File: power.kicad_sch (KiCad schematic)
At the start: 18 parts, among them U4 TPS61040DBV, U5 TPS7A2050PDBV

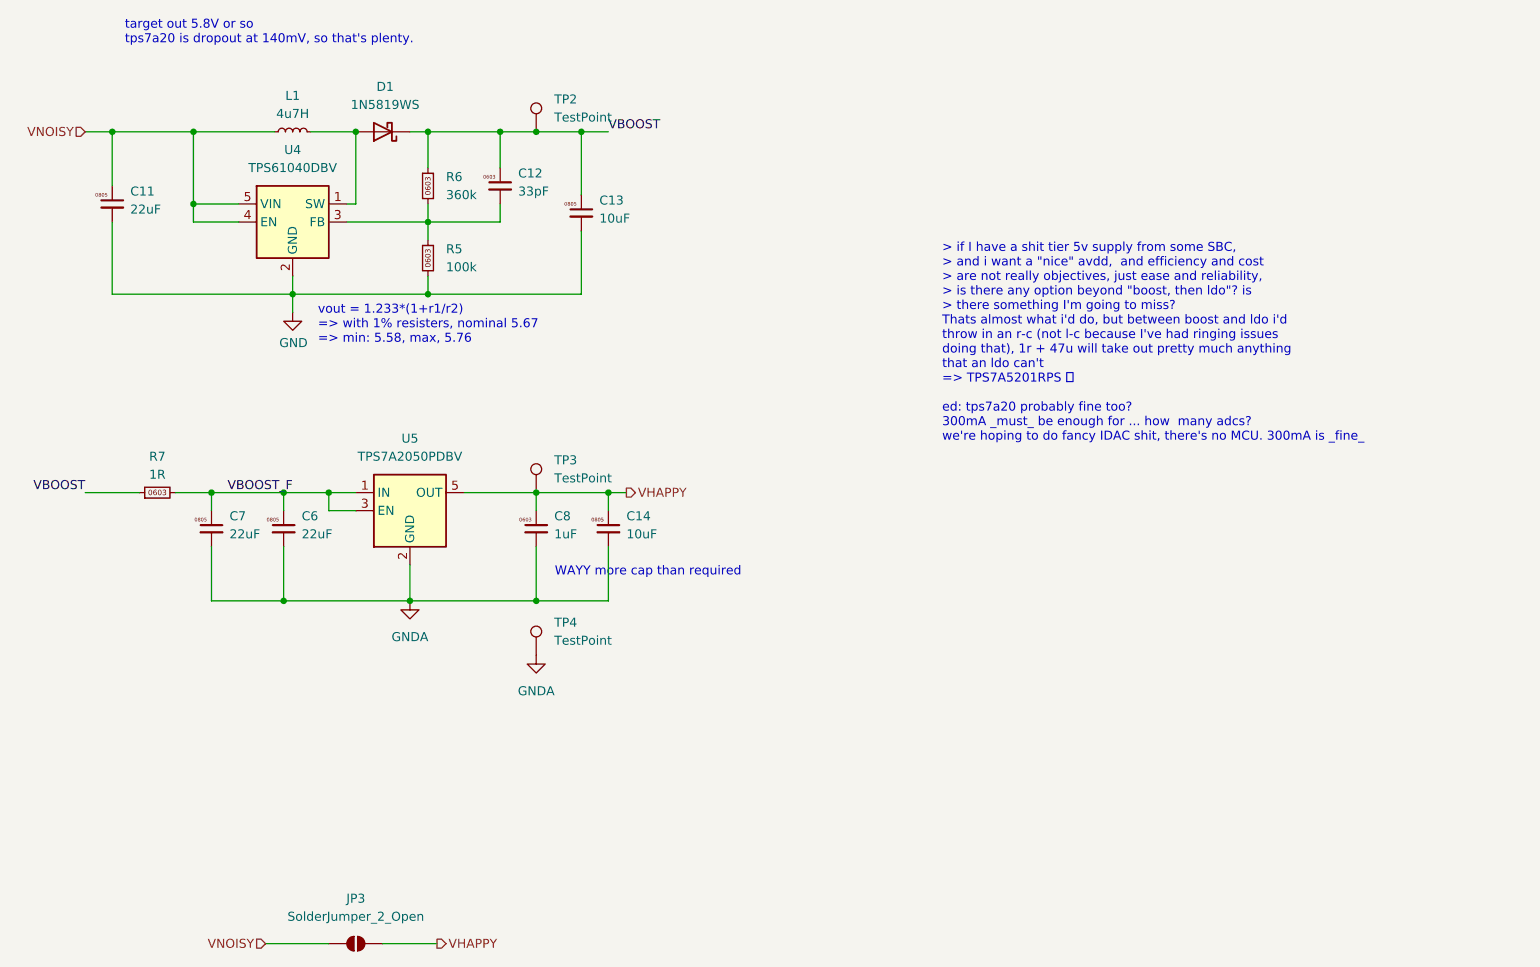
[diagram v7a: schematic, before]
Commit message: erc/drc cleanups
fix lots of off grid stuff that got dragged off in earlier
re-arrangements
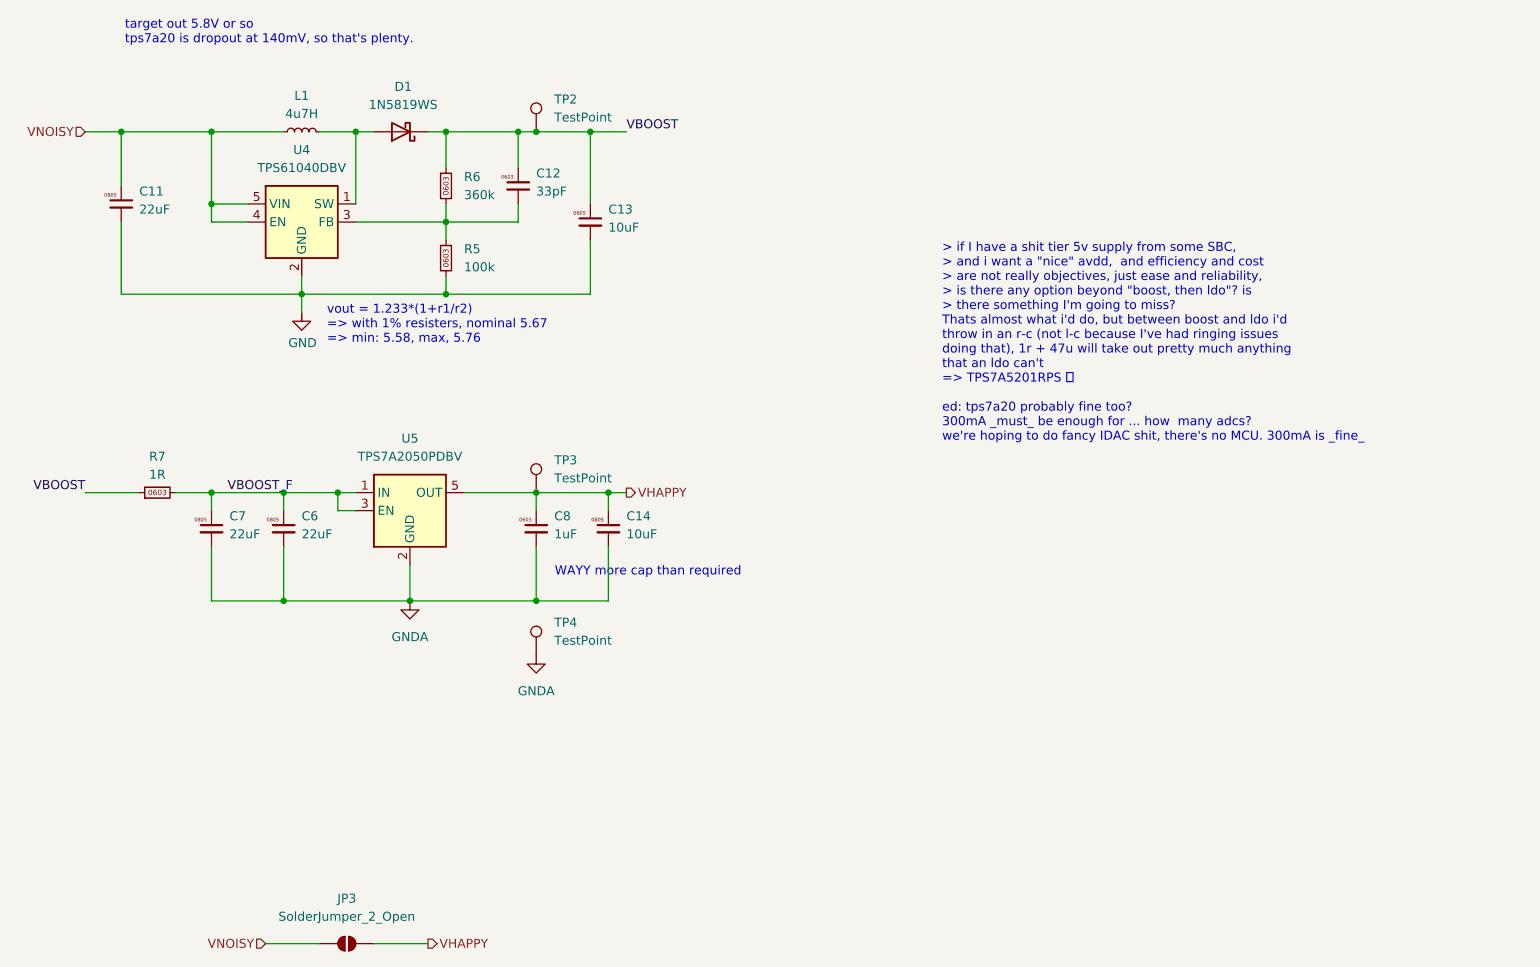
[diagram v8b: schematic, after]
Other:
- moved on the sheet: C11, C12, C13, D1, JP3, L1, R5, R6, U4
